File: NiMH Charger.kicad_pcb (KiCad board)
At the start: 2 copper layers, 78.7 x 61 mm, 23 parts, among them Q1 IRF510, Q2 IRF510, Q3 IRF510, Q4 IRF510, U1 Arduino_NANO, U2 LM7805

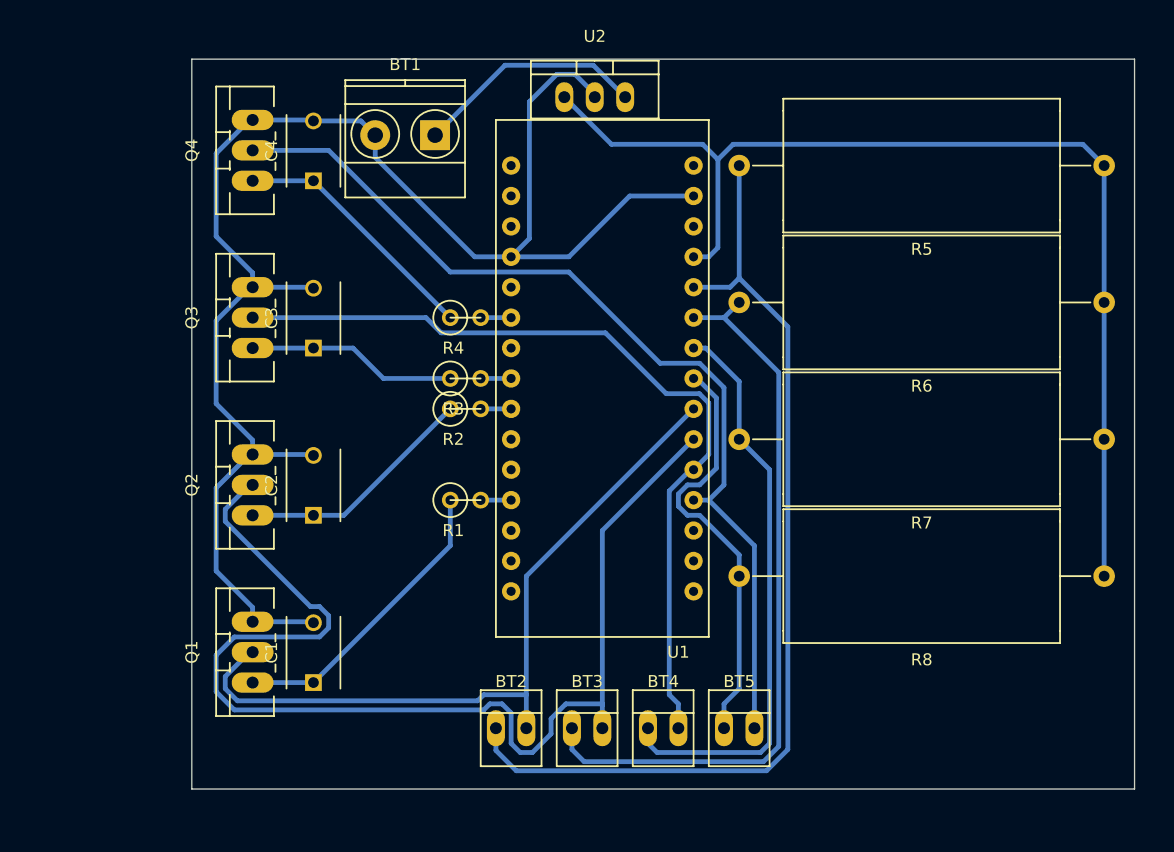
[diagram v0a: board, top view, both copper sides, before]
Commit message: Removed 7805 Voltage Regulator
Unsure whether 7805 will be able to provide the necessary current should all four cells be charging simultaneously at highest current. The circuit now relies on a regulated 5V supply voltage.
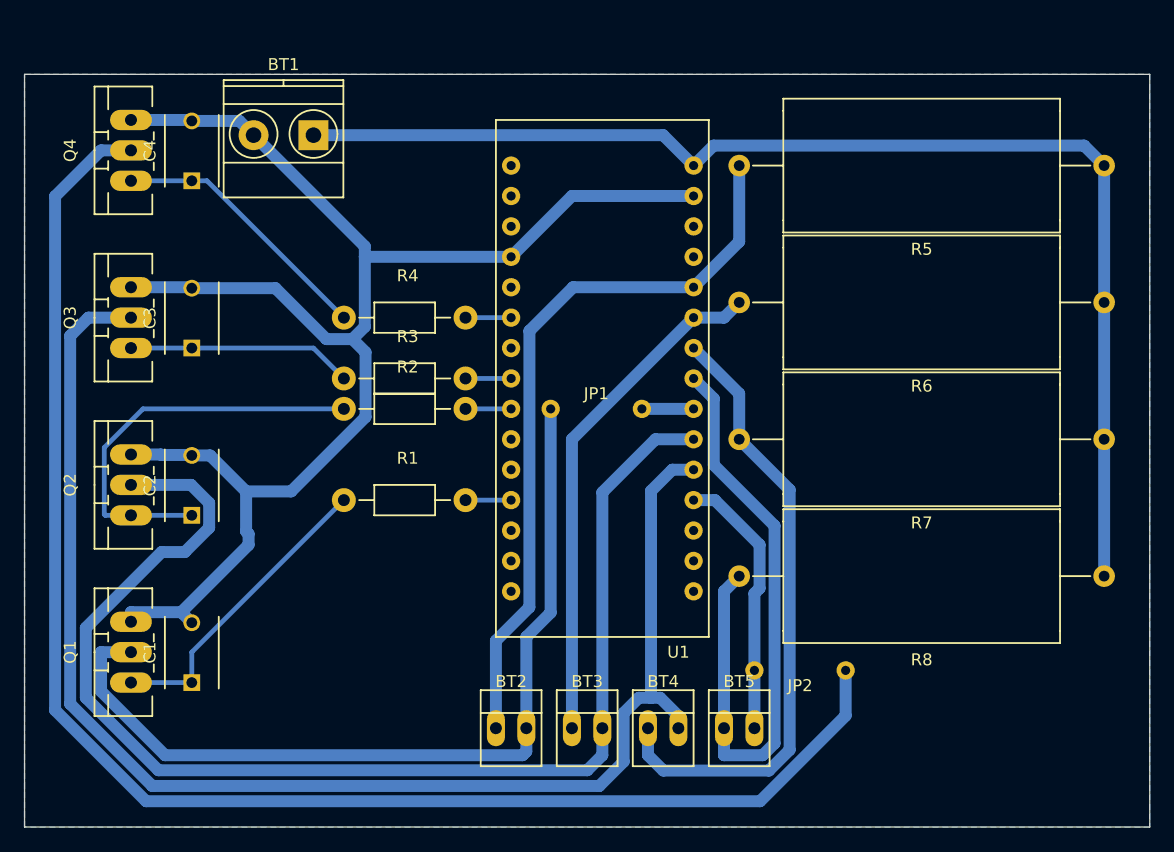
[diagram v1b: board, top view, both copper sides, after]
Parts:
- removed U2: LM7805, TO_SOT_Packages_THT:TO-220_Neutral123_Vertical
- added JP1: JUMPER, Custom:Jumper, F.Cu at (132.8, 105.4)
- added JP2: JUMPER, Custom:Jumper, F.Cu at (149.9, 127.3)
- R1, R2, R3, R4: footprint Discret:R1 -> Resistors_ThroughHole:Resistor_Horizontal_RM10mm
- moved BT1 10.2 mm to (109.2, 82.5)
- moved C1 10.2 mm to (99.1, 128.3)
- moved C2 10.2 mm to (99.1, 114.3)
- moved C3 10.2 mm to (99.1, 100.3)
- moved C4 10.2 mm to (99.1, 86.4)
- moved Q1 10.2 mm to (94.0, 125.7)
- moved Q2 10.2 mm to (94.0, 111.8)
- moved Q3 10.2 mm to (94.0, 97.8)
- moved Q4 10.2 mm to (94.0, 83.8)
- moved R1 10.2 mm to (111.8, 113.0)
- moved R2 10.2 mm to (111.8, 105.4)
- moved R3 10.2 mm to (111.8, 102.9)
- moved R4 10.2 mm to (111.8, 97.8)
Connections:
- Q4 pad 2: Net-(BT5-Pad2) -> Net-(JP2-Pad2)
- R5 pad 1: /5V -> /VIN
- R6 pad 1: /5V -> /VIN
- R7 pad 1: /5V -> /VIN
- R8 pad 1: /5V -> /VIN
- U1 pad 12: /5V -> (no net)
- U1 pad 15: (no net) -> /VIN
- U1 pad 7: Net-(BT2-Pad2) -> Net-(JP1-Pad1)
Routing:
- net Net-(JP2-Pad2): track 0.00 -> 126.8 mm
- net /5V: track 92.5 -> 0.00 mm
- net /VIN: track 19.4 -> 102.8 mm
- net Net-(BT5-Pad2): track 79.4 -> 22.8 mm
- net Net-(BT4-Pad2): track 70.0 -> 118.7 mm
- net Net-(BT2-Pad1): track 82.3 -> 61.3 mm
- net Net-(BT3-Pad1): track 62.0 -> 42.8 mm
- net Net-(BT5-Pad1): track 35.2 -> 53.4 mm
- net Net-(C2-Pad1): track 20.2 -> 34.3 mm
- net Net-(BT2-Pad2): track 62.4 -> 73.1 mm
- net Net-(BT3-Pad2): track 96.4 -> 106.4 mm
- net Net-(BT4-Pad1): track 47.4 -> 52.2 mm
- net Net-(JP1-Pad1): track 0.00 -> 4.32 mm
- net Net-(R4-Pad2): track 2.54 -> 3.81 mm
- net Net-(R3-Pad2): track 2.54 -> 3.81 mm
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- added copper zone on B.Cu, net /GND
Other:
- board size 78.7 x 61 mm -> 94 x 62.9 mm
- net class Power: clearance 0.15 -> 0.25; trace_width 0.4 -> 1
